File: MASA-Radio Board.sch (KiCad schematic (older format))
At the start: 47 parts, among them IC1 FAN4010IL6X_F113, IC2 FAN4010IL6X_F113, J1 Conn_01x02, J2 Conn_01x02_Male, J3 Conn_01x06, J4 Conn_01x03_Male, J5 SC_19-20, J6 Conn_01x06, J7 Conn_01x02, J8 UJ2-MBH-1-SMT-TR, U1 MP5077GG-Z, U2 BL654PA, U3 MIC5504-3.3YM5, U5 MP5077GG-Z

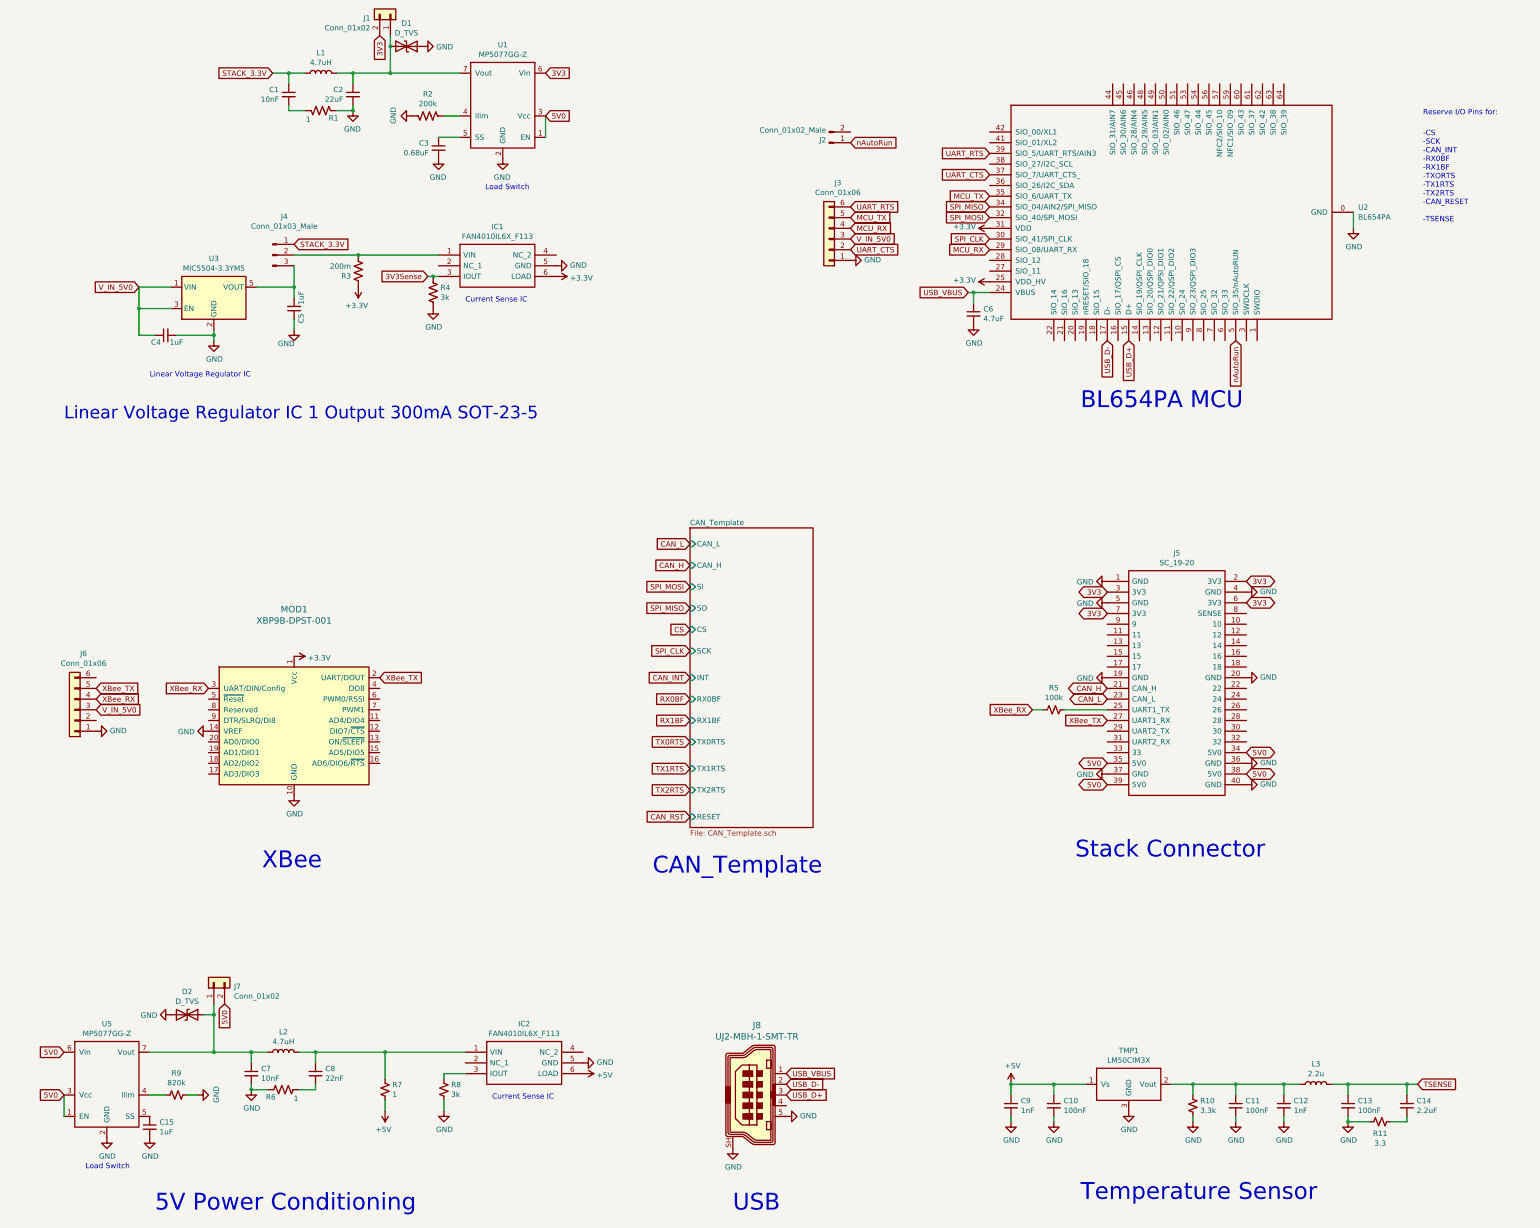
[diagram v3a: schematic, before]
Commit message: Added caps to xbee input, header to SWD pins
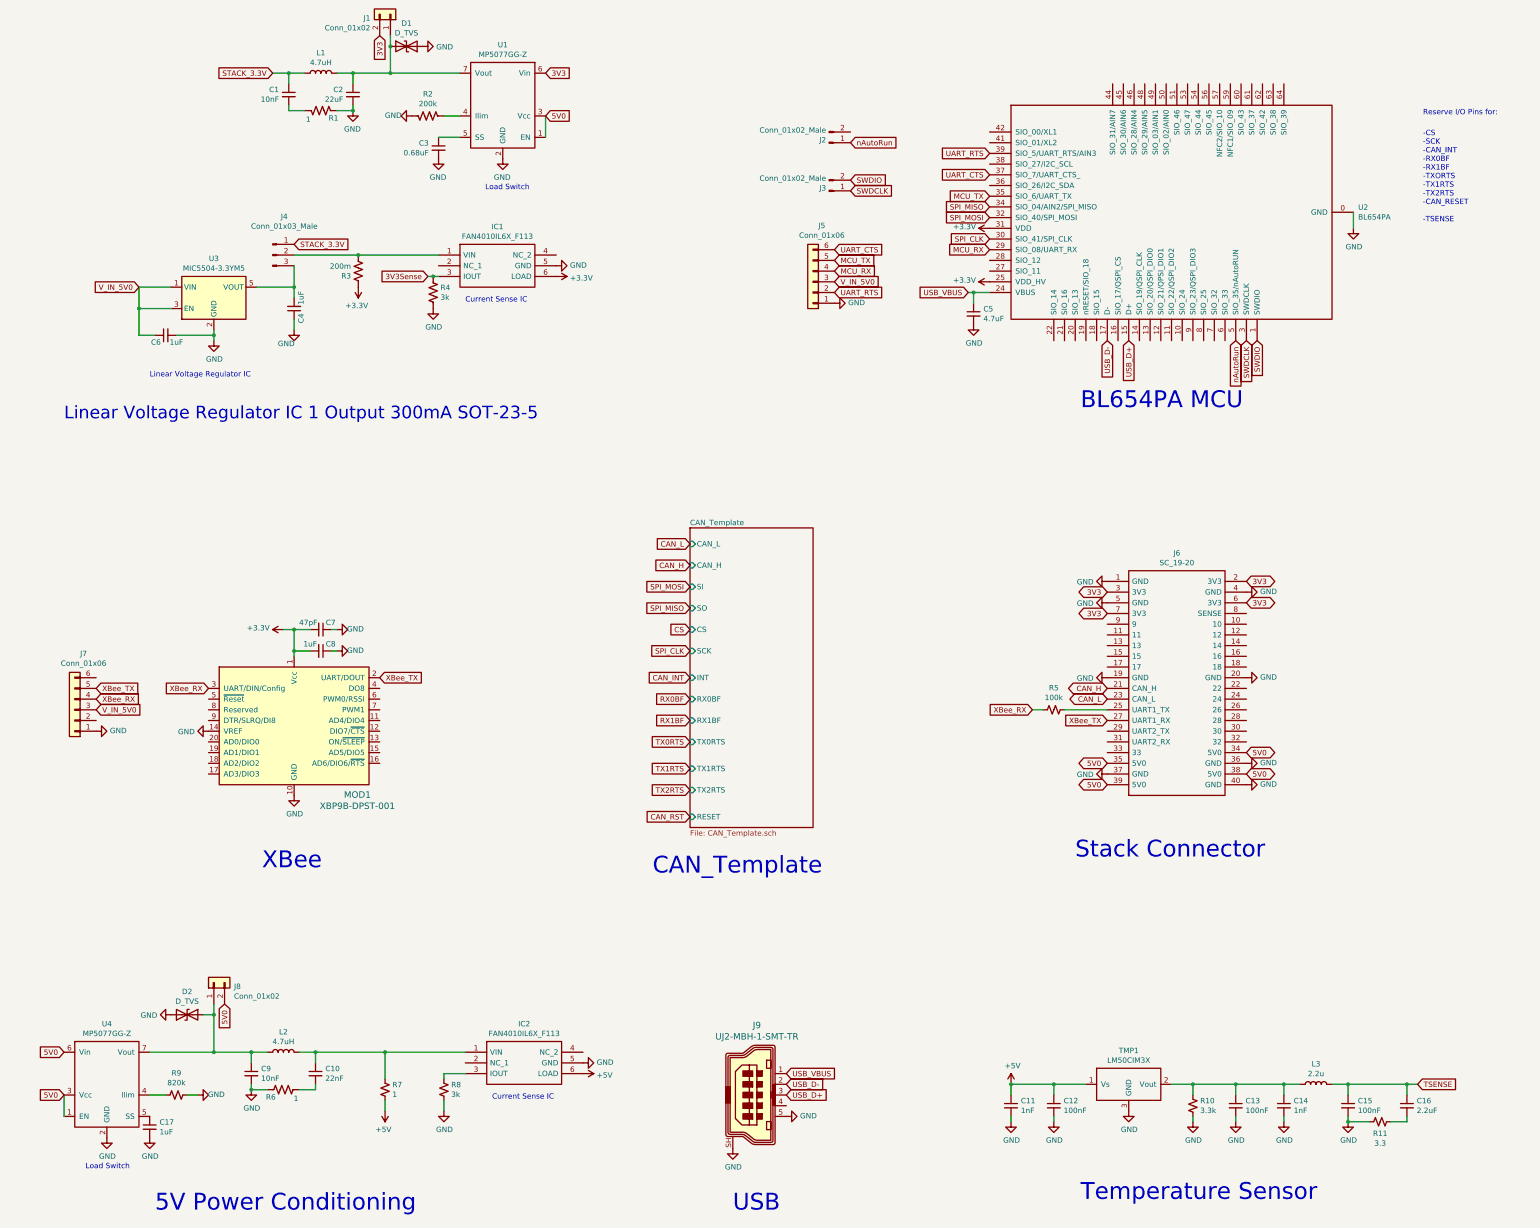
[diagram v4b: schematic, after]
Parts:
- added C7: 47pF, Capacitor_SMD:C_0805_2012Metric, symbol Device:C_Small
- added C8: 1uF, Capacitor_SMD:C_0805_2012Metric, symbol Device:C_Small
- added J3: Conn_01x02_Male, Connector_PinHeader_2.54mm:PinHeader_1x02_P2.54mm_Vertical, symbol Connector:Conn_01x02_Male
- renumbered C8 to C10, C9 to C11, C10 to C12, C11 to C13, C12 to C14, C13 to C15, C14 to C16, C15 to C17, C5 to C4, C6 to C5, C4 to C6, C7 to C9, J3 to J5, J5 to J6, J6 to J7, J7 to J8, J8 to J9, U5 to U4
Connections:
- net +3V3: now also C7.2, C8.2
- net GND: now also C7.1, C8.1
- net UART_CTS: now also J5.6 (Pin_6); no longer J5.2 (Pin_2)
- net UART_RTS: now also J5.2 (Pin_2); no longer J5.6 (Pin_6)
- net SWDIO: now reaches U2.1 (SWDIO)
- net SWDIO: now also J3.2 (Pin_2)
- net SWDCLK: now reaches U2.3 (SWDCLK)
- net SWDCLK: now also J3.1 (Pin_1)
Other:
- moved on the sheet: J5

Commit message: added solder bridges, placed a few components on board
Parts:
- J1, J8: footprint Connector_PinHeader_2.54mm:PinHeader_1x02_P2.54mm_Vertical -> Jumper:SolderJumper-2_P1.3mm_Open_TrianglePad1.0x1.5mm

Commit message: A very rough placement of components, some routing
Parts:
- C10, C11, C12, C13, C14, C15, C16, C17, C2, C3, C4, C5, C6, C7, C8: footprint Capacitor_SMD:C_0805_2012Metric -> Capacitor_SMD:C_0603_1608Metric
- R1: footprint Resistor_SMD:R_0402_1005Metric -> Resistor_SMD:R_0603_1608Metric
- R10, R11, R2, R3, R4, R5, R7, R8, R9: footprint Resistor_SMD:R_0805_2012Metric -> Resistor_SMD:R_0603_1608Metric
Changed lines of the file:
@@
 F 0 "R4" H 6318 4546 50  0000 L CNN
 F 1 "3k" H 6318 4455 50  0000 L CNN
-F 2 "Resistor_SMD:R_0805_2012Metric" V 6290 4490 50  0001 C CNN
+F 2 "Resistor_SMD:R_0603_1608Metric" V 6290 4490 50  0001 C CNN
 F 3 "~" H 6250 4500 50  0001 C CNN
 	1    6250 4500
@@
 F 0 "R3" H 5618 4346 50  0000 L CNN
 F 1 "200m" H 5618 4255 50  0000 L CNN
-F 2 "Resistor_SMD:R_0805_2012Metric" V 5590 4290 50  0001 C CNN
+F 2 "Resistor_SMD:R_0603_1608Metric" V 5590 4290 50  0001 C CNN
 F 3 "~" H 5550 4300 50  0001 C CNN
 	1    5550 4300
@@
 F 0 "C3" H 6392 3196 50  0000 L CNN
 F 1 "0.68uF" H 6392 3105 50  0000 L CNN
-F 2 "Capacitor_SMD:C_0805_2012Metric" H 6300 3150 50  0001 C CNN
+F 2 "Capacitor_SMD:C_0603_1608Metric" H 6300 3150 50  0001 C CNN
 F 3 "~" H 6300 3150 50  0001 C CNN
 	1    6300 3150
@@
 F 0 "R2" V 5995 2850 50  0000 C CNN
 F 1 "200k" V 6086 2850 50  0000 C CNN
-F 2 "Resistor_SMD:R_0805_2012Metric" V 6240 2840 50  0001 C CNN
+F 2 "Resistor_SMD:R_0603_1608Metric" V 6240 2840 50  0001 C CNN
 F 3 "~" H 6200 2850 50  0001 C CNN
 	1    6200 2850
@@
 F 0 "R1" V 5130 2918 50  0000 C CNN
 F 1 "1" V 5117 2682 50  0000 C CNN
-F 2 "Resistor_SMD:R_0402_1005Metric" V 5240 2790 50  0001 C CNN
+F 2 "Resistor_SMD:R_0603_1608Metric" V 5240 2790 50  0001 C CNN
 F 3 "~" H 5200 2800 50  0001 C CNN
 	1    5200 2800
@@
 F 0 "C2" H 5592 2696 50  0000 L CNN
 F 1 "22uF" H 5592 2605 50  0000 L CNN
-F 2 "Capacitor_SMD:C_0805_2012Metric" H 5500 2650 50  0001 C CNN
+F 2 "Capacitor_SMD:C_0603_1608Metric" H 5500 2650 50  0001 C CNN
 F 3 "~" H 5500 2650 50  0001 C CNN
 	1    5500 2650
@@
 F 0 "C17" H 3692 12346 50  0000 L CNN
 F 1 "1uF" H 3692 12255 50  0000 L CNN
-F 2 "Capacitor_SMD:C_0805_2012Metric" H 3600 12300 50  0001 C CNN
+F 2 "Capacitor_SMD:C_0603_1608Metric" H 3600 12300 50  0001 C CNN
 F 3 "~" H 3600 12300 50  0001 C CNN
 	1    3600 12300
@@
 F 0 "R9" V 3645 12000 50  0000 C CNN
 F 1 "820k" V 3736 12000 50  0000 C CNN
-F 2 "Resistor_SMD:R_0805_2012Metric" H 3850 12000 50  0001 C CNN
+F 2 "Resistor_SMD:R_0603_1608Metric" H 3850 12000 50  0001 C CNN
 F 3 "~" H 3850 12000 50  0001 C CNN
 	1    3850 12000
@@
 F 0 "C10" H 5242 11846 50  0000 L CNN
 F 1 "22nF" H 5242 11755 50  0000 L CNN
-F 2 "Capacitor_SMD:C_0805_2012Metric" H 5150 11800 50  0001 C CNN
+F 2 "Capacitor_SMD:C_0603_1608Metric" H 5150 11800 50  0001 C CNN
 F 3 "~" H 5150 11800 50  0001 C CNN
 	1    5150 11800
@@
 F 0 "R7" H 5868 11996 50  0000 L CNN
 F 1 "1" H 5868 11905 50  0000 L CNN
-F 2 "Resistor_SMD:R_0805_2012Metric" H 5800 11950 50  0001 C CNN
+F 2 "Resistor_SMD:R_0603_1608Metric" H 5800 11950 50  0001 C CNN
 F 3 "~" H 5800 11950 50  0001 C CNN
 	1    5800 11950
@@
 F 0 "R8" H 6418 11996 50  0000 L CNN
 F 1 "3k" H 6418 11905 50  0000 L CNN
-F 2 "Resistor_SMD:R_0805_2012Metric" H 6350 11950 50  0001 C CNN
+F 2 "Resistor_SMD:R_0603_1608Metric" H 6350 11950 50  0001 C CNN
 F 3 "~" H 6350 11950 50  0001 C CNN
 	1    6350 11950
@@
 F 0 "C5" H 11392 4746 50  0000 L CNN
 F 1 "4.7uF" H 11392 4655 50  0000 L CNN
-F 2 "Capacitor_SMD:C_0805_2012Metric" H 11300 4700 50  0001 C CNN
+F 2 "Capacitor_SMD:C_0603_1608Metric" H 11300 4700 50  0001 C CNN
 F 3 "~" H 11300 4700 50  0001 C CNN
 	1    11300 4700
@@
 F 0 "R5" V 11845 8400 50  0000 C CNN
 F 1 "100k" V 11936 8400 50  0000 C CNN
-F 2 "Resistor_SMD:R_0805_2012Metric" H 12050 8400 50  0001 C CNN
+F 2 "Resistor_SMD:R_0603_1608Metric" H 12050 8400 50  0001 C CNN
 F 3 "~" H 12050 8400 50  0001 C CNN
 	1    12050 8400
@@
 F 0 "C4" V 4885 4696 50  0000 L CNN
 F 1 "1uF" V 4885 4487 50  0000 L CNN
-F 2 "Capacitor_SMD:C_0805_2012Metric" H 4950 4650 50  0001 C CNN
+F 2 "Capacitor_SMD:C_0603_1608Metric" H 4950 4650 50  0001 C CNN
 F 3 "~" H 4950 4650 50  0001 C CNN
 	1    4950 4650
@@
 F 0 "C6" V 3685 4946 50  0000 L CNN
 F 1 "1uF" V 3685 4737 50  0000 L CNN
-F 2 "Capacitor_SMD:C_0805_2012Metric" H 3750 4900 50  0001 C CNN
+F 2 "Capacitor_SMD:C_0603_1608Metric" H 3750 4900 50  0001 C CNN
 F 3 "~" H 3750 4900 50  0001 C CNN
 	1    3750 4900
@@
 F 0 "C8" V 5135 7896 50  0000 L CNN
 F 1 "1uF" V 5135 7687 50  0000 L CNN
-F 2 "Capacitor_SMD:C_0805_2012Metric" H 5200 7850 50  0001 C CNN
+F 2 "Capacitor_SMD:C_0603_1608Metric" H 5200 7850 50  0001 C CNN
 F 3 "~" H 5200 7850 50  0001 C CNN
 	1    5200 7850
@@
 F 0 "C7" V 5135 7696 50  0000 L CNN
 F 1 "47pF" V 5135 7447 50  0000 L CNN
-F 2 "Capacitor_SMD:C_0805_2012Metric" H 5200 7650 50  0001 C CNN
+F 2 "Capacitor_SMD:C_0603_1608Metric" H 5200 7650 50  0001 C CNN
 F 3 "~" H 5200 7650 50  0001 C CNN
 	1    5200 7650
@@
 F 0 "C16" H 15442 12146 50  0000 L CNN
 F 1 "2.2uF" H 15442 12055 50  0000 L CNN
-F 2 "Capacitor_SMD:C_0805_2012Metric" H 15350 12100 50  0001 C CNN
+F 2 "Capacitor_SMD:C_0603_1608Metric" H 15350 12100 50  0001 C CNN
 F 3 "~" H 15350 12100 50  0001 C CNN
 	1    15350 12100
@@
 F 0 "R11" V 14990 12250 50  0000 C CNN
 F 1 "3.3" V 14899 12250 50  0000 C CNN
-F 2 "Resistor_SMD:R_0805_2012Metric" H 15100 12250 50  0001 C CNN
+F 2 "Resistor_SMD:R_0603_1608Metric" H 15100 12250 50  0001 C CNN
 F 3 "~" H 15100 12250 50  0001 C CNN
 	1    15100 12250
@@
 F 0 "C15" H 14892 12146 50  0000 L CNN
 F 1 "100nF" H 14892 12055 50  0000 L CNN
-F 2 "Capacitor_SMD:C_0805_2012Metric" H 14800 12100 50  0001 C CNN
+F 2 "Capacitor_SMD:C_0603_1608Metric" H 14800 12100 50  0001 C CNN
 F 3 "~" H 14800 12100 50  0001 C CNN
 	1    14800 12100
@@
 F 0 "C14" H 14292 12146 50  0000 L CNN
 F 1 "1nF" H 14292 12055 50  0000 L CNN
-F 2 "Capacitor_SMD:C_0805_2012Metric" H 14200 12100 50  0001 C CNN
+F 2 "Capacitor_SMD:C_0603_1608Metric" H 14200 12100 50  0001 C CNN
 F 3 "~" H 14200 12100 50  0001 C CNN
 	1    14200 12100
@@
 F 0 "C13" H 13842 12146 50  0000 L CNN
 F 1 "100nF" H 13842 12055 50  0000 L CNN
-F 2 "Capacitor_SMD:C_0805_2012Metric" H 13750 12100 50  0001 C CNN
+F 2 "Capacitor_SMD:C_0603_1608Metric" H 13750 12100 50  0001 C CNN
 F 3 "~" H 13750 12100 50  0001 C CNN
 	1    13750 12100
@@
 F 0 "R10" H 13418 12146 50  0000 L CNN
 F 1 "3.3k" H 13418 12055 50  0000 L CNN
-F 2 "Resistor_SMD:R_0805_2012Metric" H 13350 12100 50  0001 C CNN
+F 2 "Resistor_SMD:R_0603_1608Metric" H 13350 12100 50  0001 C CNN
 F 3 "~" H 13350 12100 50  0001 C CNN
 	1    13350 12100
@@
 F 0 "C11" H 11742 12146 50  0000 L CNN
 F 1 "1nF" H 11742 12055 50  0000 L CNN
-F 2 "Capacitor_SMD:C_0805_2012Metric" H 11650 12100 50  0001 C CNN
+F 2 "Capacitor_SMD:C_0603_1608Metric" H 11650 12100 50  0001 C CNN
 F 3 "~" H 11650 12100 50  0001 C CNN
 	1    11650 12100
@@
 F 0 "C12" H 12142 12146 50  0000 L CNN
 F 1 "100nF" H 12142 12055 50  0000 L CNN
-F 2 "Capacitor_SMD:C_0805_2012Metric" H 12050 12100 50  0001 C CNN
+F 2 "Capacitor_SMD:C_0603_1608Metric" H 12050 12100 50  0001 C CNN
 F 3 "~" H 12050 12100 50  0001 C CNN
 	1    12050 12100

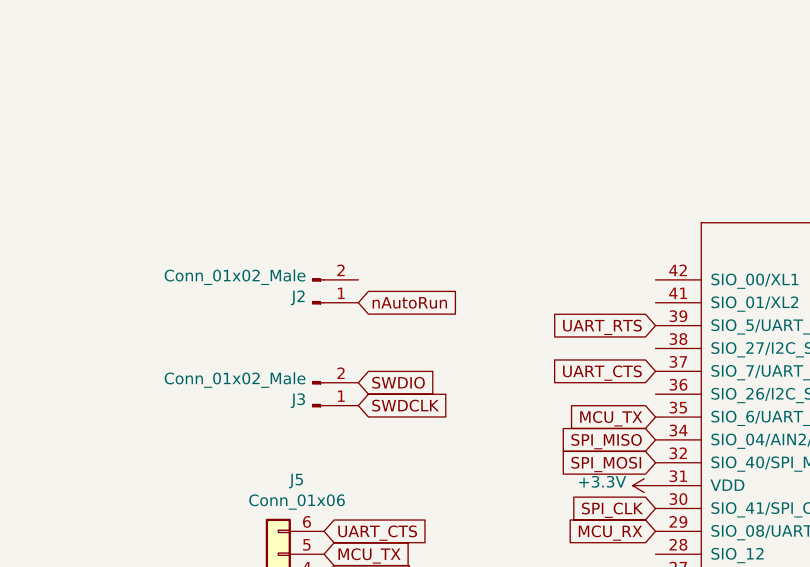
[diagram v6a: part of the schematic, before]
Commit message: Completed Most of the routing on board
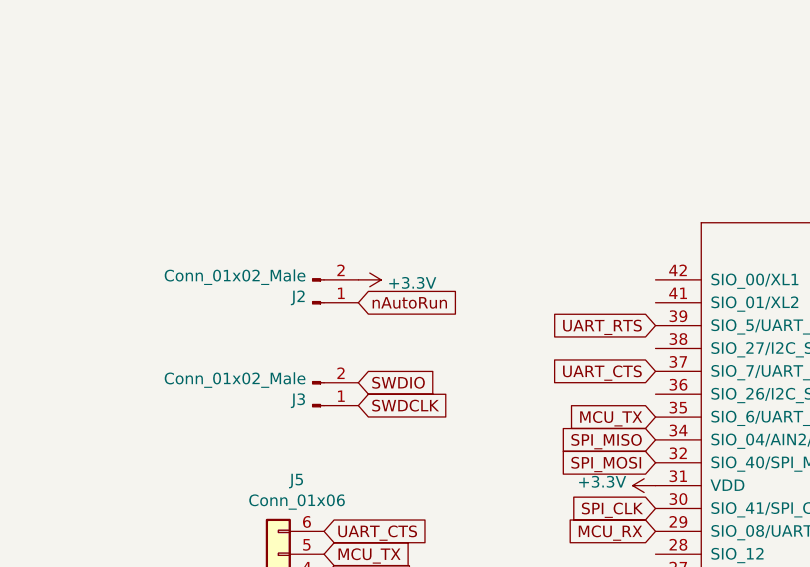
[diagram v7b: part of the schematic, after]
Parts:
- L1, L2, L3: footprint Inductor_SMD:L_0805_2012Metric -> Inductor_SMD:L_0603_1608Metric
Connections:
- net +3V3: now also J2.2 (Pin_2)
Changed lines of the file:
@@
 F 0 "L1" V 5390 2450 50  0000 C CNN
 F 1 "4.7uH" V 5299 2450 50  0000 C CNN
-F 2 "Inductor_SMD:L_0805_2012Metric" H 5200 2450 50  0001 C CNN
+F 2 "Inductor_SMD:L_0603_1608Metric" H 5200 2450 50  0001 C CNN
 F 3 "~" H 5200 2450 50  0001 C CNN
 	1    5200 2450
@@
 F 0 "L2" V 5040 11600 50  0000 C CNN
 F 1 "4.7uH" V 4949 11600 50  0000 C CNN
-F 2 "Inductor_SMD:L_0805_2012Metric" H 4850 11600 50  0001 C CNN
+F 2 "Inductor_SMD:L_0603_1608Metric" H 4850 11600 50  0001 C CNN
 F 3 "~" H 4850 11600 50  0001 C CNN
 	1    4850 11600
@@
 F 0 "L3" V 14690 11900 50  0000 C CNN
 F 1 "2.2u" V 14599 11900 50  0000 C CNN
-F 2 "Inductor_SMD:L_0805_2012Metric" H 14500 11900 50  0001 C CNN
+F 2 "Inductor_SMD:L_0603_1608Metric" H 14500 11900 50  0001 C CNN
 F 3 "~" H 14500 11900 50  0001 C CNN
 	1    14500 11900
@@
 Text GLabel 9550 12000 2    50   Input ~ 0
 USB_D+
+$Comp
+L power:+3.3V #PWR?
+U 1 1 5E65F90C
+P 10150 3000
+F 0 "#PWR?" H 10150 2850 50  0001 C CNN
+F 1 "+3.3V" V 10165 3128 50  0000 L CNN
+F 2 "" H 10150 3000 50  0001 C CNN
+F 3 "" H 10150 3000 50  0001 C CNN
+	1    10150 3000
+	0    1    1    0
+$EndComp
 $EndSCHEMATC
